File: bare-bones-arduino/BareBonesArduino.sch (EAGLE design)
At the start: 26 parts, among them J1 FTDI FT232, J3 ANALOG IN, J4 POWER, J5 DIGITAL (PWM), J6 DIGITAL (PWM), J7 POWER_JACK, U1 328P, U2 LM7805CT, U3 LM1117T-3.3, Y1 16MHz

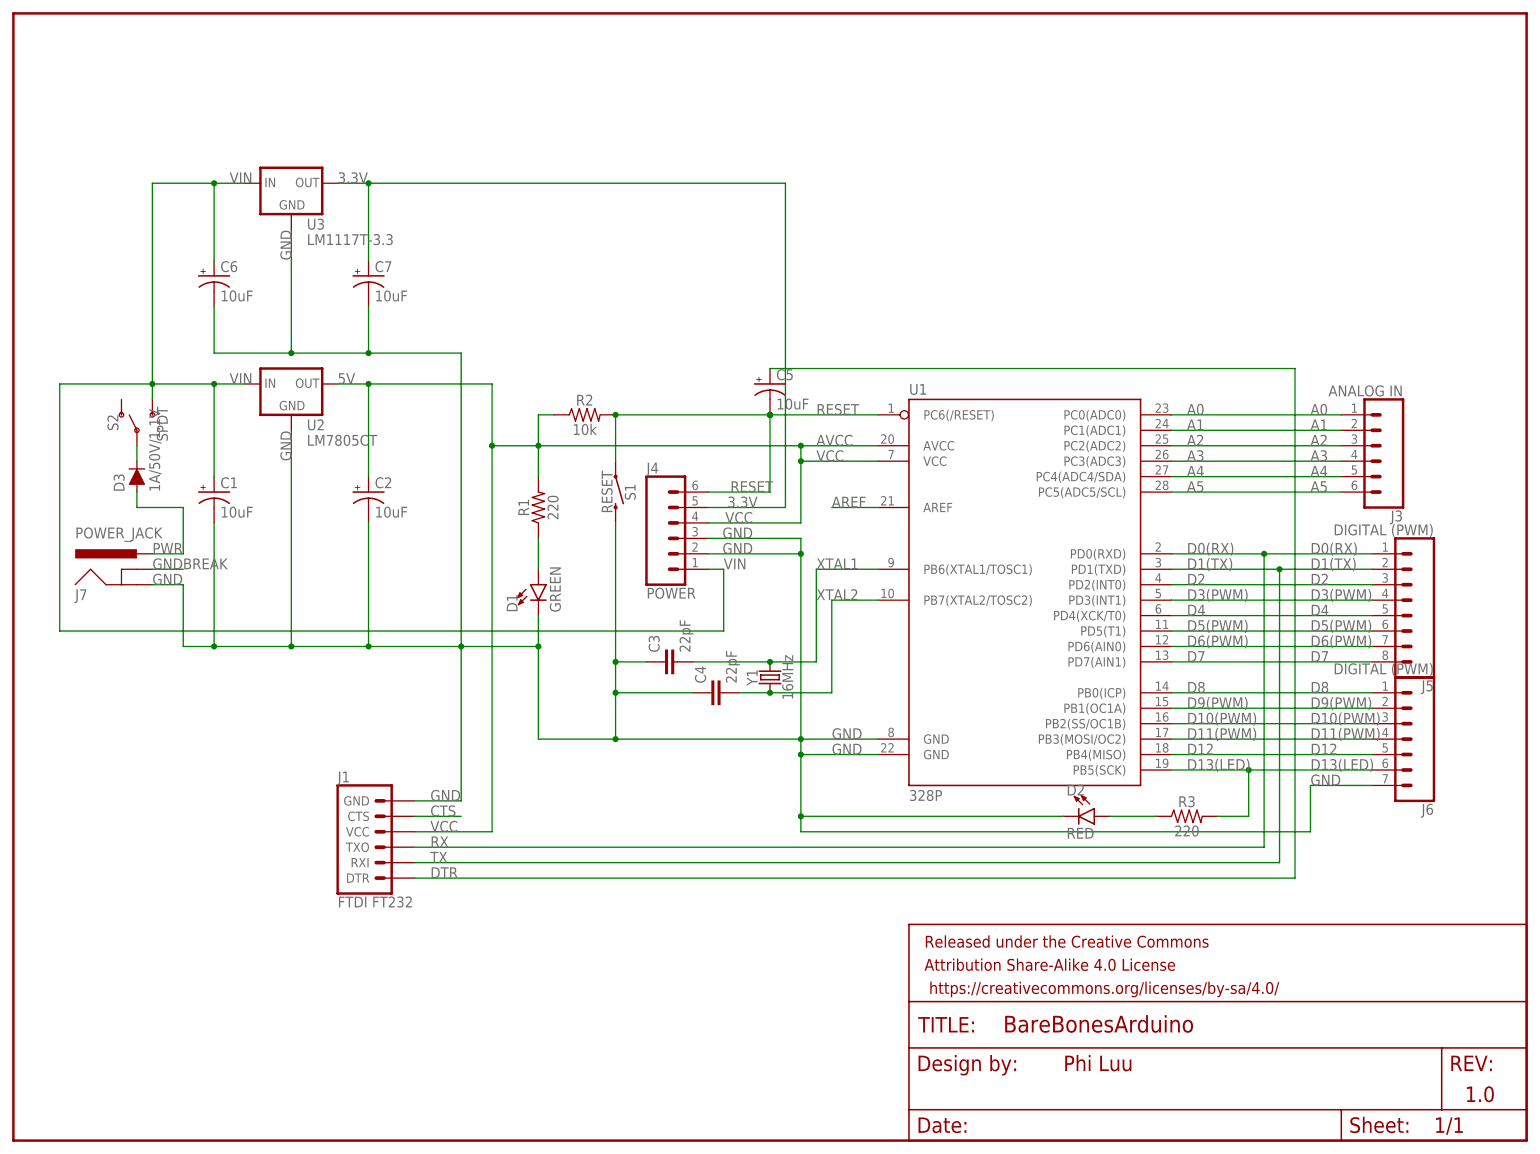
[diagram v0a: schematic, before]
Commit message: Follow naming convention - English letter only
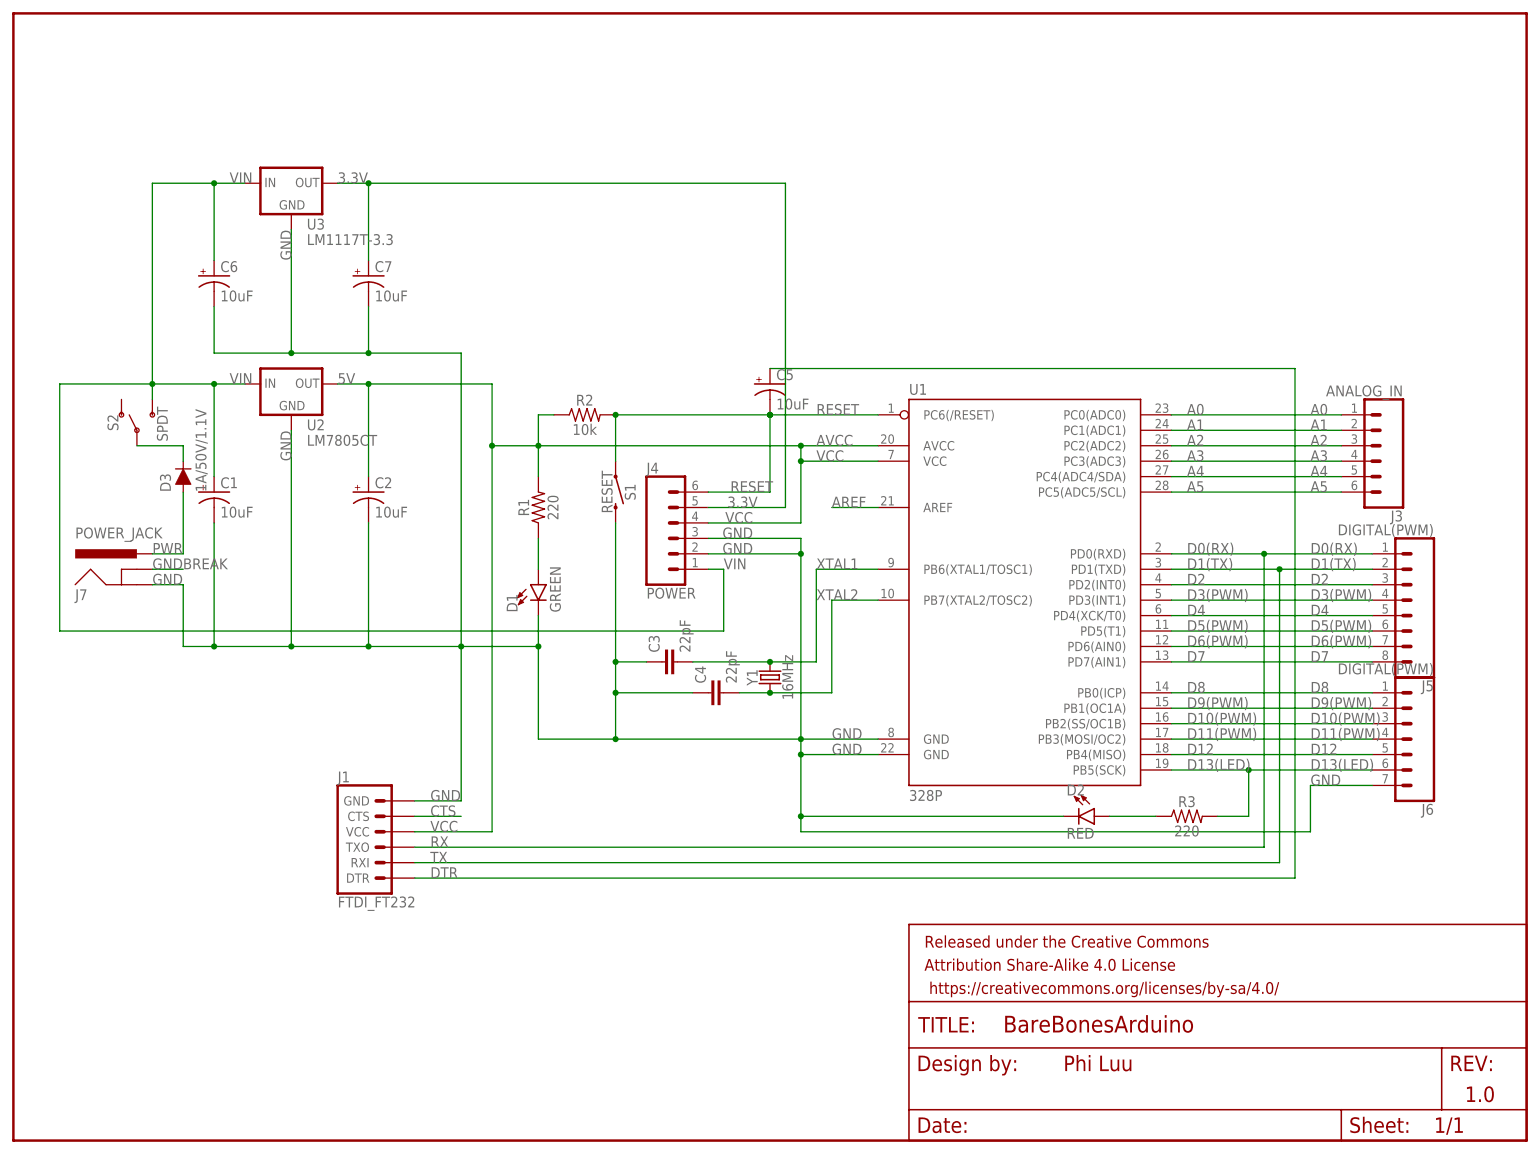
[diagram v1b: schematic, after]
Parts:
- J1: value FTDI FT232 -> FTDI_FT232
- J3: value ANALOG IN -> ANALOG_IN
- J5, J6: value DIGITAL (PWM) -> DIGITAL(PWM)
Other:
- moved on the sheet: D3
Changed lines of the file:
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@@
 <setting verticaltext="up"/>
 </settings>
-<grid distance="0.1" unitdist="inch" unit="inch" style="lines" multiple="1" display="no" altdistance="0.01" altunitdist="inch" altunit="inch"/>
+<grid distance="0.1" unitdist="inch" unit="inch" style="lines" multiple="1" display="yes" altdistance="0.01" altunitdist="inch" altunit="inch"/>
 <layers>
 <layer number="1" name="Top" color="4" fill="1" visible="no" active="no"/>
@@
 <part name="FRAME1" library="SparkFun-Aesthetics" deviceset="FRAME-LETTER" device=""/>
 <part name="U1" library="SparkFun-IC-Microcontroller" deviceset="ATMEGA328P_PDIP" device="" value="328P"/>
-<part name="J1" library="SparkFun-Connectors" deviceset="6_PIN_SERIAL_TARGET" device="" value="FTDI FT232"/>
+<part name="J1" library="SparkFun-Connectors" deviceset="6_PIN_SERIAL_TARGET" device="" value="FTDI_FT232"/>
 <part name="U2" library="SparkFun-IC-Power" deviceset="V_REG_78XX" device="-TO-220" value="LM7805CT"/>
 <part name="C1" library="SparkFun-Capacitors" deviceset="10UF-POLAR" device="-RADIAL-2.5MM-25V-20%" value="10uF"/>
@@
 <part name="D2" library="SparkFun-LED" deviceset="LED" device="5MM" value="RED"/>
 <part name="R3" library="SparkFun-Resistors" deviceset="1KOHM" device="-HORIZ-1/4W-5%" value="220"/>
-<part name="J3" library="SparkFun-Connectors" deviceset="CONN_06" device="SILK_FEMALE_PTH" value="ANALOG IN"/>
+<part name="J3" library="SparkFun-Connectors" deviceset="CONN_06" device="SILK_FEMALE_PTH" value="ANALOG_IN"/>
 <part name="J4" library="SparkFun-Connectors" deviceset="CONN_06" device="SILK_FEMALE_PTH" value="POWER"/>
-<part name="J5" library="SparkFun-Connectors" deviceset="CONN_08" device="&quot;" value="DIGITAL (PWM)"/>
-<part name="J6" library="SparkFun-Connectors" deviceset="CONN_07" device="" value="DIGITAL (PWM)"/>
+<part name="J5" library="SparkFun-Connectors" deviceset="CONN_08" device="&quot;" value="DIGITAL(PWM)"/>
+<part name="J6" library="SparkFun-Connectors" deviceset="CONN_07" device="" value="DIGITAL(PWM)"/>
 <part name="D3" library="SparkFun-DiscreteSemi" deviceset="DIODE" device="-PTH" value="1A/50V/1.1V"/>
 <part name="S2" library="SparkFun-Switches" deviceset="SWITCH-SPDT" device="-PTH-11.6X4.0MM" value="SPDT"/>
@@
 <instance part="J5" gate="G$1" x="228.6" y="88.9" rot="R180"/>
 <instance part="J6" gate="G$1" x="228.6" y="68.58" rot="R180"/>
-<instance part="D3" gate="G$1" x="20.32" y="109.22" rot="R90"/>
+<instance part="D3" gate="G$1" x="27.94" y="109.22" rot="R90"/>
 <instance part="S2" gate="1" x="20.32" y="116.84" rot="R90"/>
 <instance part="J7" gate="G$1" x="20.32" y="88.9"/>
@@
 </segment>
 </net>
-<net name="N$2" class="0">
-<segment>
-<pinref part="S2" gate="1" pin="P"/>
-<pinref part="D3" gate="G$1" pin="C"/>
-<wire x1="20.32" y1="114.3" x2="20.32" y2="111.76" width="0.1524" layer="91"/>
-</segment>
-</net>
 <net name="GNDBREAK" class="0">
 <segment>
@@
 <label x="22.86" y="96.52" size="1.778" layer="95"/>
 <pinref part="D3" gate="G$1" pin="A"/>
-<wire x1="20.32" y1="106.68" x2="20.32" y2="104.14" width="0.1524" layer="91"/>
-<wire x1="20.32" y1="104.14" x2="27.94" y2="104.14" width="0.1524" layer="91"/>
-<wire x1="27.94" y1="104.14" x2="27.94" y2="96.52" width="0.1524" layer="91"/>
-</segment>
-</net>
+<wire x1="27.94" y1="106.68" x2="27.94" y2="96.52" width="0.1524" layer="91"/>
+</segment>
+</net>
+<net name="N$2" class="0">
+<segment>
+<pinref part="S2" gate="1" pin="P"/>
+<pinref part="D3" gate="G$1" pin="C"/>
+<wire x1="20.32" y1="114.3" x2="27.94" y2="114.3" width="0.1524" layer="91"/>
+<wire x1="27.94" y1="114.3" x2="27.94" y2="111.76" width="0.1524" layer="91"/>
+</segment>
+</net>
